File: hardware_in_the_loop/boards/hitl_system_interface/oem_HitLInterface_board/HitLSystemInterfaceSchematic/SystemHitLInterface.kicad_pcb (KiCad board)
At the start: 2 copper layers, 60 x 60 mm, 54 parts, among them J1 CONN_02X03, J2 Conn_01x04_Female, J3 Conn_01x04_Female, J4 Barrel_Jack, J5 Conn_01x04_Female, J6 Conn_01x01_Female, J7 Conn_01x01_Female, J8 Conn_01x01_Female, U1 ATmega328P-AU, U101 TPS560430YF, U3 USB_MicroB, U4 FT232RL, U6 NanoFit_RA_TH_12, Y1 Crystal_SMD

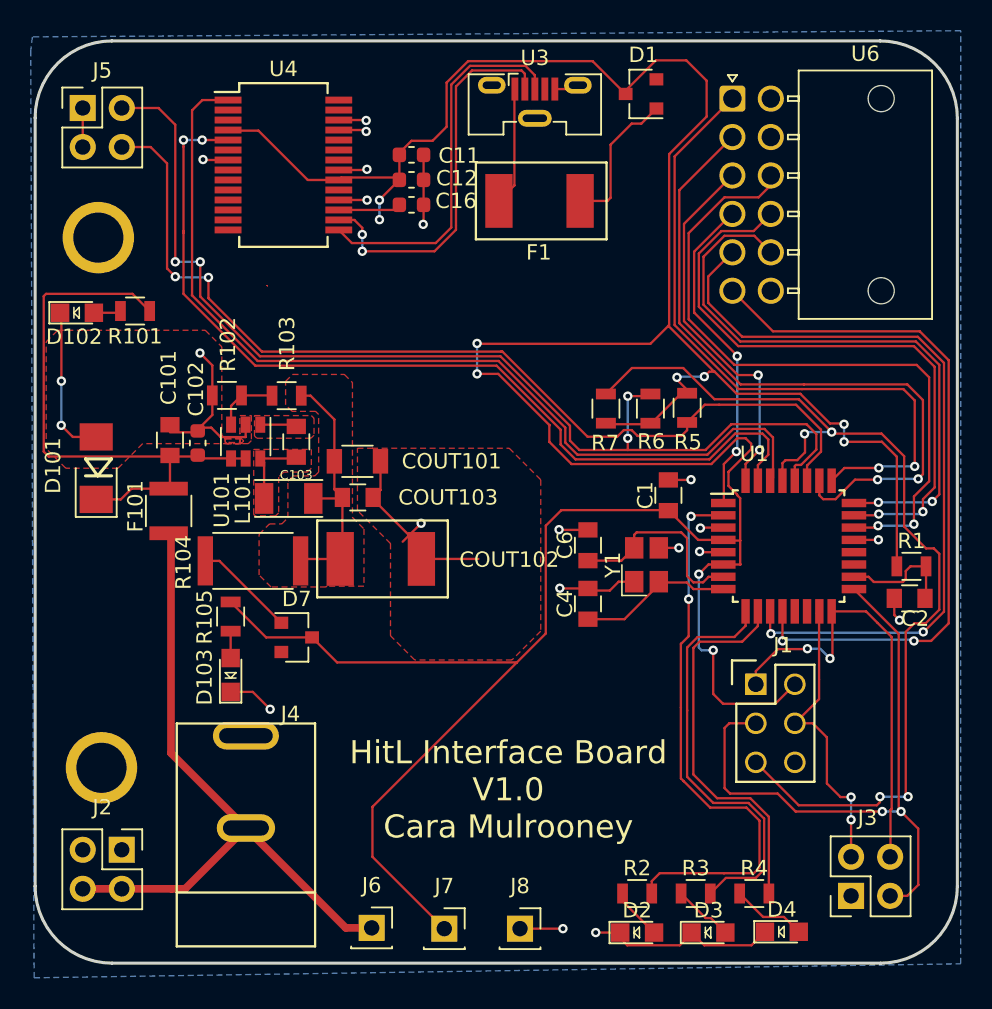
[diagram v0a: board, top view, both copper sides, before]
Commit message: Updated Fuse and Zener Diode on Buck Converter
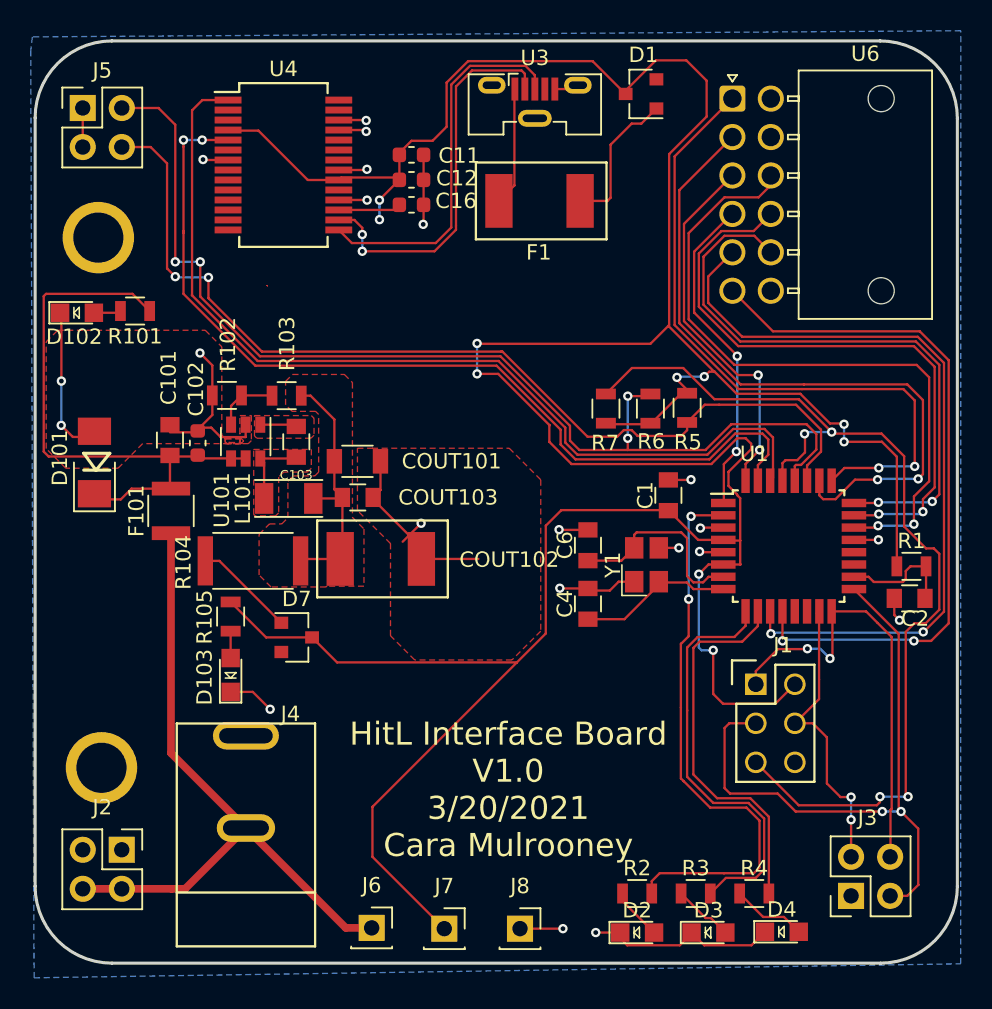
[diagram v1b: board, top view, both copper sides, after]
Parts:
- moved D101 0.39 mm to (102.4, 103.1)
- moved F101 0.15 mm to (107.3, 106.2), turned to 90 degrees
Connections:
- F101 pad 1: Net-(C101-Pad1) -> /12V
- F101 pad 2: /12V -> Net-(C101-Pad1)
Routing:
- net GND: track 88.5 -> 87.5 mm
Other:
- board text added: "HitL Interface Board V1.0 3/20/2021 Cara Mulrooney"
- board text removed: "HitL Interface Board V1.0 Cara Mulrooney"
